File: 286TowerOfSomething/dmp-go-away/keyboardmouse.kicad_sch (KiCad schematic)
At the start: 1 part, among them U1 M6117C

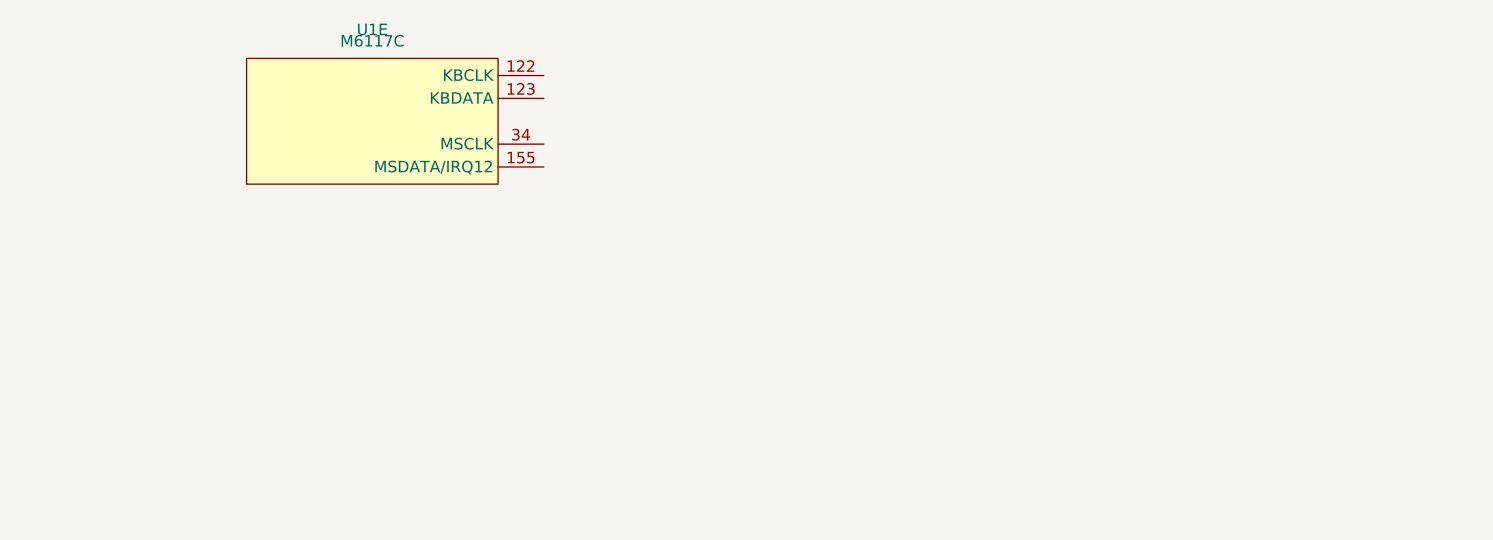
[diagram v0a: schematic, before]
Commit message: Adding keyboard/mouse and oscillator to schematic of dmp-go-away
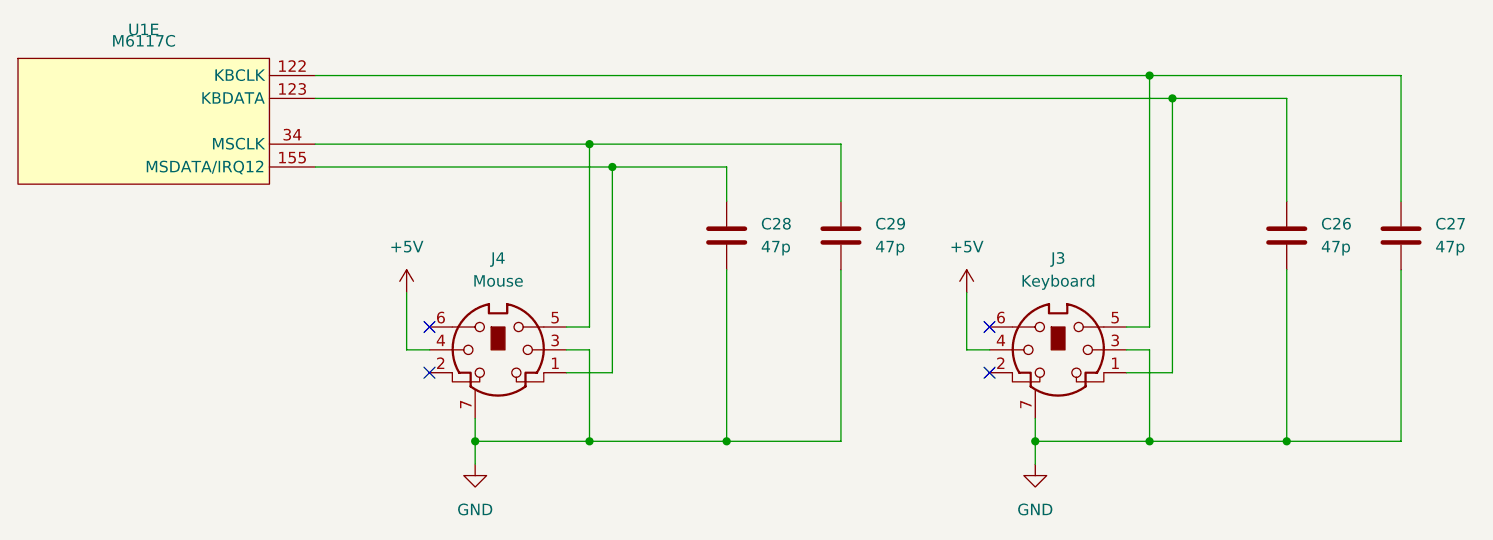
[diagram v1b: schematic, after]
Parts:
- added C26, C27, C28, C29: 47p, symbol Device:C
- added J3: Keyboard, symbol pc-parts:Mini-DIN-6
- added J4: Mouse, symbol pc-parts:Mini-DIN-6
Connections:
- net at U1.122 (KBCLK): now also C27.1, J3.5
- net at U1.123 (KBDATA): now also C26.1, J3.1
- net at U1.155 (MSDATA/IRQ12): now also C28.1, J4.1
- net at U1.34 (MSCLK): now also C29.1, J4.5
- new net +5V: J3.4, J4.4
- new net GND: C26.2, C27.2, C28.2, C29.2, J3.3, J3.7, J4.3, J4.7
- no-connect marks 0 -> 4
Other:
- moved on the sheet: U1E

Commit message: Added footprints and started figuring out layout for dmp-go-away
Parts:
- C26, C27, C28, C29: footprint (none) -> Capacitor_SMD:C_0603_1608Metric_Pad1.08x0.95mm_HandSolder
- J3, J4: footprint (none) -> pc-parts:CUI_MD-60SGK
- U1: footprint (none) -> Package_QFP:PQFP-208_28x28mm_P0.5mm
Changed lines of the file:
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@@
 			)
 		)
-		(property "Footprint" ""
+		(property "Footprint" "pc-parts:CUI_MD-60SGK"
 			(at 203.2 127 0)
 			(effects
@@
 			)
 		)
-		(property "Footprint" ""
+		(property "Footprint" "Capacitor_SMD:C_0603_1608Metric_Pad1.08x0.95mm_HandSolder"
 			(at 242.2652 118.11 0)
 			(effects
@@
 			)
 		)
-		(property "Footprint" ""
+		(property "Footprint" "Capacitor_SMD:C_0603_1608Metric_Pad1.08x0.95mm_HandSolder"
 			(at 229.5652 118.11 0)
 			(effects
@@
 			)
 		)
-		(property "Footprint" ""
+		(property "Footprint" "Package_QFP:PQFP-208_28x28mm_P0.5mm"
 			(at 101.6 101.6 0)
 			(effects
@@
 			)
 		)
-		(property "Footprint" ""
+		(property "Footprint" "Capacitor_SMD:C_0603_1608Metric_Pad1.08x0.95mm_HandSolder"
 			(at 180.0352 118.11 0)
 			(effects
@@
 			)
 		)
-		(property "Footprint" ""
+		(property "Footprint" "pc-parts:CUI_MD-60SGK"
 			(at 140.97 127 0)
 			(effects
@@
 			)
 		)
-		(property "Footprint" ""
+		(property "Footprint" "Capacitor_SMD:C_0603_1608Metric_Pad1.08x0.95mm_HandSolder"
 			(at 167.3352 118.11 0)
 			(effects
